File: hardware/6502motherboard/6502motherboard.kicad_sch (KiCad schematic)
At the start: 21 parts, among them J1 AUX 5VDC, J2 POWER 5V, J3 GND, SW1 POWER, U3 74HCT273

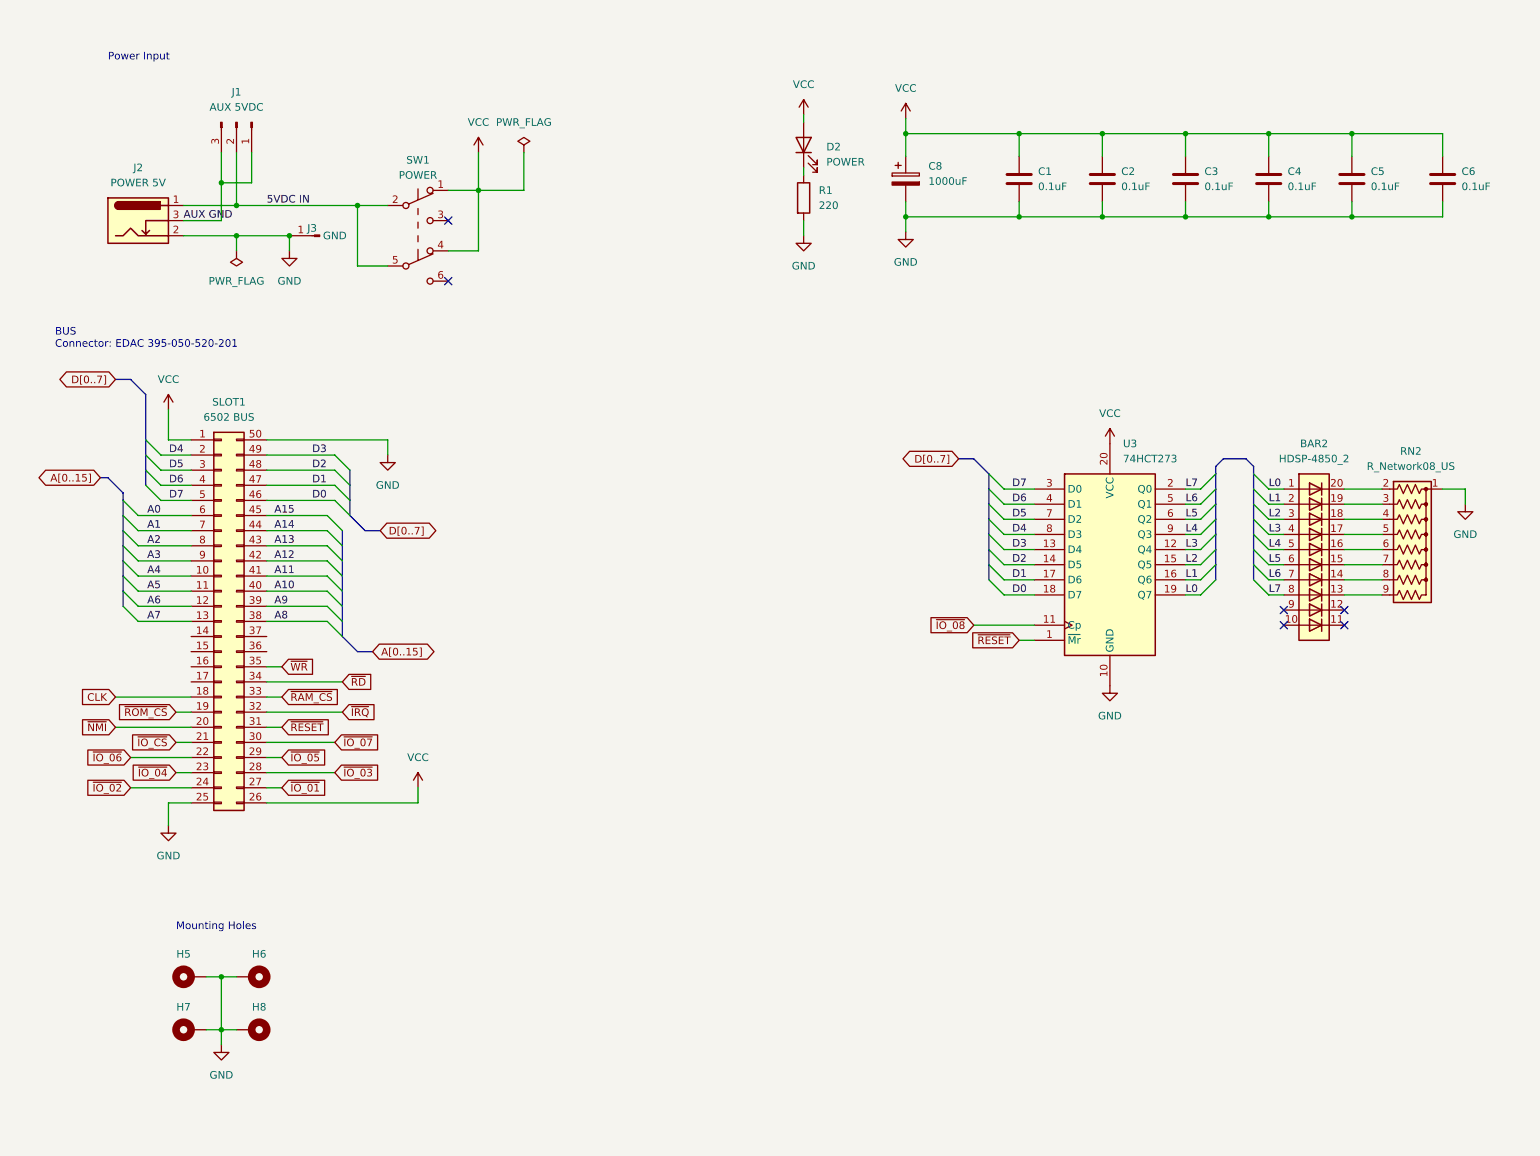
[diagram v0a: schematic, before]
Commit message: Fixed 6502 Pinout, routed bus and power
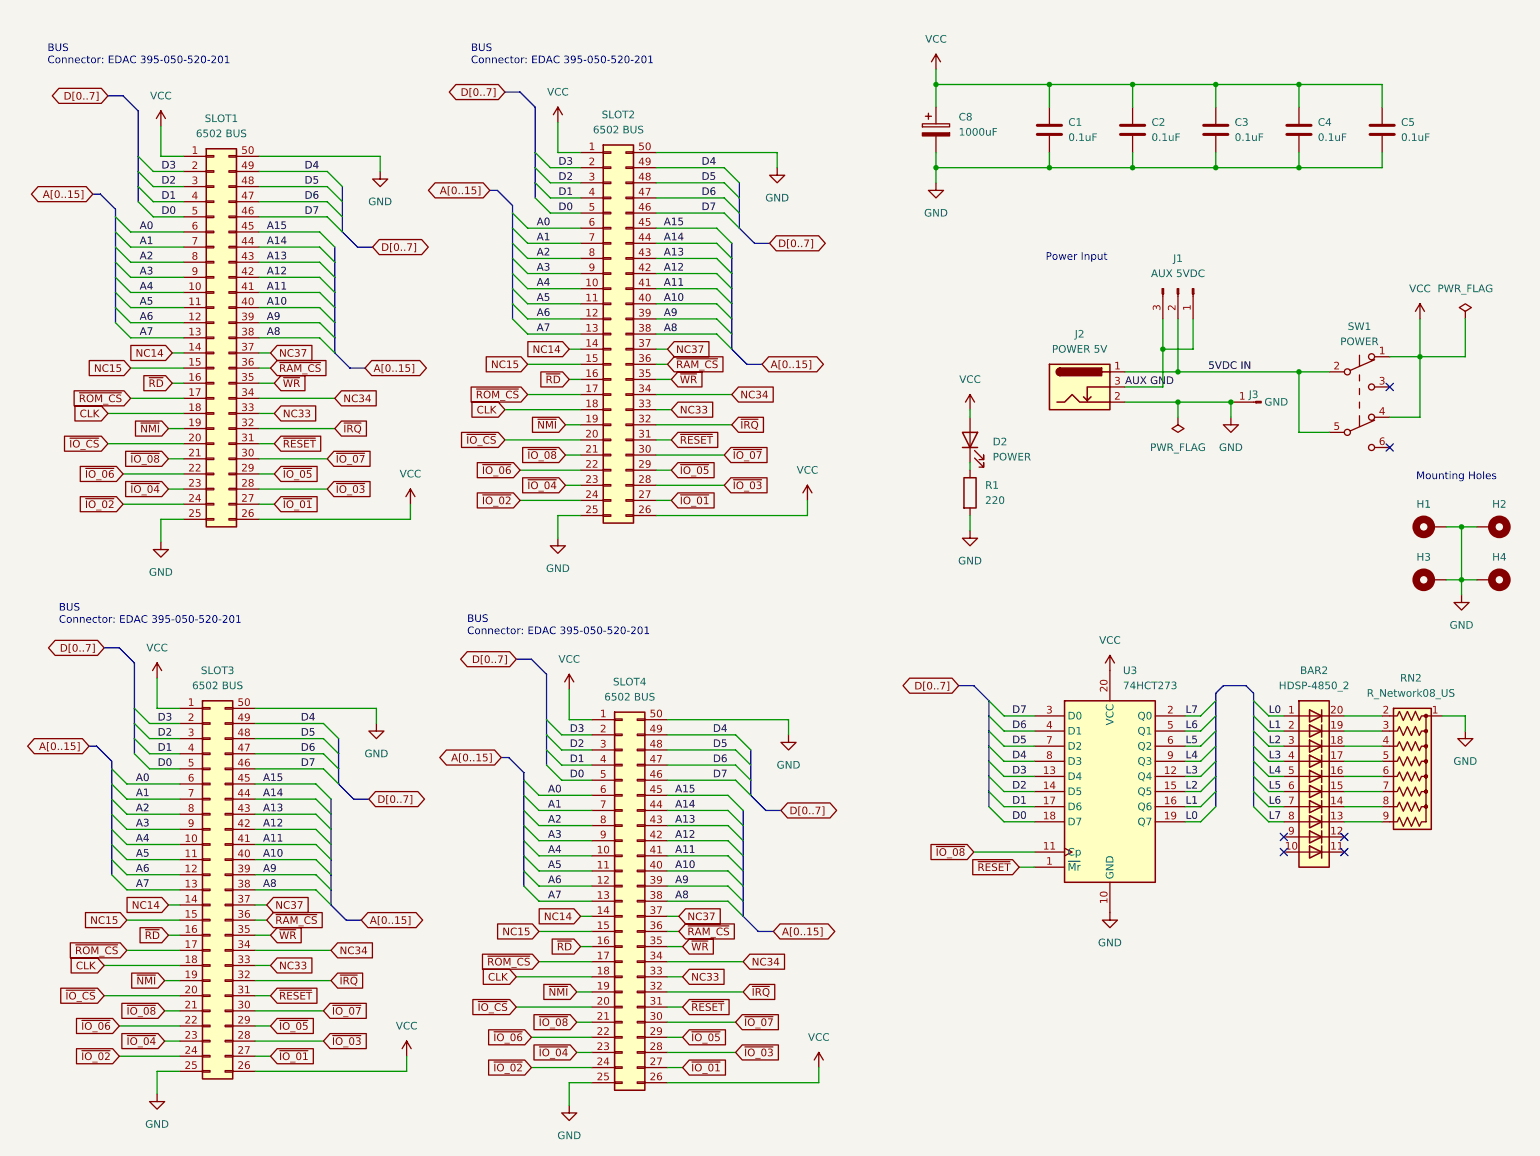
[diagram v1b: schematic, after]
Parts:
- removed C6: 0.1uF, Capacitor_THT:C_Disc_D3.0mm_W1.6mm_P2.50mm, symbol Device:C
- added SLOT2, SLOT3, SLOT4: 6502 BUS, Connector_Card:EDAC 395-050-520-201, symbol Connector_Generic:Conn_02x25_Counter_Clockwise
- renumbered H5 to H1, H6 to H2, H7 to H3, H8 to H4
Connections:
- net A0: now also SLOT2.6 (Pin_6), SLOT3.6 (Pin_6), SLOT4.6 (Pin_6)
- net A1: now also SLOT2.7 (Pin_7), SLOT3.7 (Pin_7), SLOT4.7 (Pin_7)
- net A10: now also SLOT2.40 (Pin_40), SLOT3.40 (Pin_40), SLOT4.40 (Pin_40)
- net A11: now also SLOT2.41 (Pin_41), SLOT3.41 (Pin_41), SLOT4.41 (Pin_41)
- net A12: now also SLOT2.42 (Pin_42), SLOT3.42 (Pin_42), SLOT4.42 (Pin_42)
- net A13: now also SLOT2.43 (Pin_43), SLOT3.43 (Pin_43), SLOT4.43 (Pin_43)
- net A14: now also SLOT2.44 (Pin_44), SLOT3.44 (Pin_44), SLOT4.44 (Pin_44)
- net A15: now also SLOT2.45 (Pin_45), SLOT3.45 (Pin_45), SLOT4.45 (Pin_45)
- net A2: now also SLOT2.8 (Pin_8), SLOT3.8 (Pin_8), SLOT4.8 (Pin_8)
- net A3: now also SLOT2.9 (Pin_9), SLOT3.9 (Pin_9), SLOT4.9 (Pin_9)
- net A4: now also SLOT2.10 (Pin_10), SLOT3.10 (Pin_10), SLOT4.10 (Pin_10)
- net A5: now also SLOT2.11 (Pin_11), SLOT3.11 (Pin_11), SLOT4.11 (Pin_11)
- net A6: now also SLOT2.12 (Pin_12), SLOT3.12 (Pin_12), SLOT4.12 (Pin_12)
- net A7: now also SLOT2.13 (Pin_13), SLOT3.13 (Pin_13), SLOT4.13 (Pin_13)
- net A8: now also SLOT2.38 (Pin_38), SLOT3.38 (Pin_38), SLOT4.38 (Pin_38)
- net A9: now also SLOT2.39 (Pin_39), SLOT3.39 (Pin_39), SLOT4.39 (Pin_39)
- net CLK: now also SLOT2.18 (Pin_18), SLOT3.18 (Pin_18), SLOT4.18 (Pin_18)
- net D0: now also SLOT1.5 (Pin_5), SLOT2.5 (Pin_5), SLOT3.5 (Pin_5), SLOT4.5 (Pin_5); no longer SLOT1.46 (Pin_46)
- net D1: now also SLOT1.4 (Pin_4), SLOT2.4 (Pin_4), SLOT3.4 (Pin_4), SLOT4.4 (Pin_4); no longer SLOT1.47 (Pin_47)
- net D2: now also SLOT1.3 (Pin_3), SLOT2.3 (Pin_3), SLOT3.3 (Pin_3), SLOT4.3 (Pin_3); no longer SLOT1.48 (Pin_48)
- net D3: now also SLOT1.2 (Pin_2), SLOT2.2 (Pin_2), SLOT3.2 (Pin_2), SLOT4.2 (Pin_2); no longer SLOT1.49 (Pin_49)
- net D4: now also SLOT1.49 (Pin_49), SLOT2.49 (Pin_49), SLOT3.49 (Pin_49), SLOT4.49 (Pin_49); no longer SLOT1.2 (Pin_2)
- net D5: now also SLOT1.48 (Pin_48), SLOT2.48 (Pin_48), SLOT3.48 (Pin_48), SLOT4.48 (Pin_48); no longer SLOT1.3 (Pin_3)
- net D6: now also SLOT1.47 (Pin_47), SLOT2.47 (Pin_47), SLOT3.47 (Pin_47), SLOT4.47 (Pin_47); no longer SLOT1.4 (Pin_4)
- net D7: now also SLOT1.46 (Pin_46), SLOT2.46 (Pin_46), SLOT3.46 (Pin_46), SLOT4.46 (Pin_46); no longer SLOT1.5 (Pin_5)
- net GND: now also SLOT2.25 (Pin_25), SLOT2.50 (Pin_50), SLOT3.25 (Pin_25), SLOT3.50 (Pin_50), SLOT4.25 (Pin_25), SLOT4.50 (Pin_50)
- net VCC: now also SLOT2.1 (Pin_1), SLOT2.26 (Pin_26), SLOT3.1 (Pin_1), SLOT3.26 (Pin_26), SLOT4.1 (Pin_1), SLOT4.26 (Pin_26)
- net ~{IO_01}: now also SLOT2.27 (Pin_27), SLOT3.27 (Pin_27), SLOT4.27 (Pin_27)
- net ~{IO_02}: now also SLOT2.24 (Pin_24), SLOT3.24 (Pin_24), SLOT4.24 (Pin_24)
- net ~{IO_03}: now also SLOT2.28 (Pin_28), SLOT3.28 (Pin_28), SLOT4.28 (Pin_28)
- net ~{IO_04}: now also SLOT2.23 (Pin_23), SLOT3.23 (Pin_23), SLOT4.23 (Pin_23)
- net ~{IO_05}: now also SLOT2.29 (Pin_29), SLOT3.29 (Pin_29), SLOT4.29 (Pin_29)
- net ~{IO_06}: now also SLOT2.22 (Pin_22), SLOT3.22 (Pin_22), SLOT4.22 (Pin_22)
- net ~{IO_07}: now also SLOT2.30 (Pin_30), SLOT3.30 (Pin_30), SLOT4.30 (Pin_30)
- net ~{IO_08}: now also SLOT1.21 (Pin_21), SLOT2.21 (Pin_21), SLOT3.21 (Pin_21), SLOT4.21 (Pin_21)
- net ~{IO_CS}: now also SLOT1.20 (Pin_20), SLOT2.20 (Pin_20), SLOT3.20 (Pin_20), SLOT4.20 (Pin_20); no longer SLOT1.21 (Pin_21)
- net ~{IRQ}: now also SLOT2.32 (Pin_32), SLOT3.32 (Pin_32), SLOT4.32 (Pin_32)
- net ~{NMI}: now also SLOT1.19 (Pin_19), SLOT2.19 (Pin_19), SLOT3.19 (Pin_19), SLOT4.19 (Pin_19); no longer SLOT1.20 (Pin_20)
- net ~{RAM_CS}: now also SLOT1.36 (Pin_36), SLOT2.36 (Pin_36), SLOT3.36 (Pin_36), SLOT4.36 (Pin_36); no longer SLOT1.33 (Pin_33)
- net ~{RD}: now also SLOT1.16 (Pin_16), SLOT2.16 (Pin_16), SLOT3.16 (Pin_16), SLOT4.16 (Pin_16); no longer SLOT1.34 (Pin_34)
- net ~{RESET}: now also SLOT2.31 (Pin_31), SLOT3.31 (Pin_31), SLOT4.31 (Pin_31)
- net ~{ROM_CS}: now also SLOT1.17 (Pin_17), SLOT2.17 (Pin_17), SLOT3.17 (Pin_17), SLOT4.17 (Pin_17); no longer SLOT1.19 (Pin_19)
- net ~{WR}: now also SLOT2.35 (Pin_35), SLOT3.35 (Pin_35), SLOT4.35 (Pin_35)
- net NC14: now reaches SLOT1.14 (Pin_14)
- net NC14: now also SLOT2.14 (Pin_14), SLOT3.14 (Pin_14), SLOT4.14 (Pin_14)
- net NC15: now reaches SLOT1.15 (Pin_15)
- net NC15: now also SLOT2.15 (Pin_15), SLOT3.15 (Pin_15), SLOT4.15 (Pin_15)
- net NC37: now reaches SLOT1.37 (Pin_37)
- net NC37: now also SLOT2.37 (Pin_37), SLOT3.37 (Pin_37), SLOT4.37 (Pin_37)
- new net NC33: SLOT1.33 (Pin_33), SLOT2.33 (Pin_33), SLOT3.33 (Pin_33), SLOT4.33 (Pin_33)
- new net NC34: SLOT1.34 (Pin_34), SLOT2.34 (Pin_34), SLOT3.34 (Pin_34), SLOT4.34 (Pin_34)
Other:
- moved on the sheet: BAR2, C1, C2, C3, C4, C5, C8, D2, H1, H2, H3, H4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

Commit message: v1.0 Motherboard Ready
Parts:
- added SW2: SW_Push, Button_Switch_THT:SW_PUSH_6mm_H5mm, symbol Switch:SW_Push
- added T1: DS-1813, Package_TO_SOT_THT:21-0248A_MAXIM, symbol Mariano Extras:DS-1813
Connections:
- net GND: now also SW2.2, T1.3 (GND)
- net VCC: now also T1.2 (VCC)
- net ~{RESET}: now also SW2.1, T1.1 (~{RST})
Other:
- moved on the sheet: D2, R1

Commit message: v1.6 Motherboard Complete
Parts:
- removed D2: POWER, LED_THT:LED_D3.0mm, symbol Device:LED
- removed R1: 220, Resistor_THT:R_Axial_DIN0204_L3.6mm_D1.6mm_P7.62mm_Horizontal, symbol Device:R
- added R2: 220, Resistor_THT:R_Axial_DIN0204_L3.6mm_D1.6mm_P7.62mm_Horizontal, symbol Device:R
- added SLOT5: 6502 BUS, Connector_PinHeader_2.54mm:PinHeader_2x25_P2.54mm_Vertical_Counter_Clockwise, symbol Connector_Generic:Conn_02x25_Counter_Clockwise
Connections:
- net A0: now also SLOT5.6 (Pin_6)
- net A1: now also SLOT5.7 (Pin_7)
- net A10: now also SLOT5.40 (Pin_40)
- net A11: now also SLOT5.41 (Pin_41)
- net A12: now also SLOT5.42 (Pin_42)
- net A13: now also SLOT5.43 (Pin_43)
- net A14: now also SLOT5.44 (Pin_44)
- net A15: now also SLOT5.45 (Pin_45)
- net A2: now also SLOT5.8 (Pin_8)
- net A3: now also SLOT5.9 (Pin_9)
- net A4: now also SLOT5.10 (Pin_10)
- net A5: now also SLOT5.11 (Pin_11)
- net A6: now also SLOT5.12 (Pin_12)
- net A7: now also SLOT5.13 (Pin_13)
- net A8: now also SLOT5.38 (Pin_38)
- net A9: now also SLOT5.39 (Pin_39)
- net CLK: now also SLOT5.18 (Pin_18)
- net D0: now also SLOT5.5 (Pin_5)
- net D1: now also SLOT5.4 (Pin_4)
- net D2: now also SLOT5.3 (Pin_3)
- net D3: now also SLOT5.2 (Pin_2)
- net D4: now also SLOT5.49 (Pin_49)
- net D5: now also SLOT5.48 (Pin_48)
- net D6: now also SLOT5.47 (Pin_47)
- net D7: now also SLOT5.46 (Pin_46)
- net GND: now also R2.2, SLOT5.25 (Pin_25), SLOT5.50 (Pin_50)
- net NC14: now also SLOT5.14 (Pin_14)
- net NC15: now also SLOT5.15 (Pin_15)
- net NC33: now also SLOT5.33 (Pin_33)
- net NC34: now also SLOT5.34 (Pin_34)
- net NC37: now also SLOT5.37 (Pin_37)
- net VCC: now also BAR2.11 (K), SLOT5.1 (Pin_1), SLOT5.26 (Pin_26)
- net ~{IO_01}: now also SLOT5.27 (Pin_27)
- net ~{IO_02}: now also SLOT5.24 (Pin_24)
- net ~{IO_03}: now also SLOT5.28 (Pin_28)
- net ~{IO_04}: now also SLOT5.23 (Pin_23)
- net ~{IO_05}: now also SLOT5.29 (Pin_29)
- net ~{IO_06}: now also SLOT5.22 (Pin_22)
- net ~{IO_07}: now also SLOT5.30 (Pin_30)
- net ~{IO_08}: now also SLOT5.21 (Pin_21)
- net ~{IO_CS}: now also SLOT5.20 (Pin_20)
- net ~{IRQ}: now also SLOT5.32 (Pin_32)
- net ~{NMI}: now also SLOT5.19 (Pin_19)
- net ~{RAM_CS}: now also SLOT5.36 (Pin_36)
- net ~{RD}: now also SLOT5.16 (Pin_16)
- net ~{RESET}: now also SLOT5.31 (Pin_31)
- net ~{ROM_CS}: now also SLOT5.17 (Pin_17)
- net ~{WR}: now also SLOT5.35 (Pin_35)
- net at BAR2.10 (A): now also R2.1
- no-connect marks 6 -> 4
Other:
- moved on the sheet: BAR2, C1, C2, C3, C4, C5, C8, H1, H2, H3, H4, J1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

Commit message: Motherboard added 7805 regulator
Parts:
- added C6: 100nF, Capacitor_THT:C_Disc_D3.0mm_W1.6mm_P2.50mm, symbol Device:C_Small
- added C7: 330nF, Capacitor_THT:C_Disc_D3.0mm_W1.6mm_P2.50mm, symbol Device:C_Small
- added J4: NO 7502, Connector_PinHeader_2.54mm:PinHeader_1x03_P2.54mm_Vertical, symbol Connector:Conn_01x03_Pin
- added U1: LM7805_TO220, Package_TO_SOT_THT:TO-220-3_Horizontal_TabDown, symbol Regulator_Linear:LM7805_TO220
- C8: value 1000uF -> 10uF
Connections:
- net GND: now also C6.2, C7.2, U1.2 (GND)
- net VCC: now also BAR2.10 (A), C6.1, J4.3 (Pin_3), U1.3 (VO); no longer BAR2.11 (K), SW1.1 (A), SW1.4 (A)
- net at R2.1: now also BAR2.11 (K); no longer BAR2.10 (A)
- net 5VDC IN renamed VDC
- new net VDC_IN: J4.2 (Pin_2), SW1.1 (A), SW1.4 (A)
- new net V_IN: C7.1, J4.1 (Pin_1), U1.1 (VI)
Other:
- moved on the sheet: J1, J2, J3, R2, SW1

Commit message: I_O8 Jumper and more PCB cleanup
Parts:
- added J5: IO_8, Connector_PinHeader_2.54mm:PinHeader_1x02_P2.54mm_Vertical, symbol Connector:Conn_01x02_Pin
- U1: value LM7805_TO220 -> LM7805
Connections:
- net ~{IO_08}: now also J5.2 (Pin_2); no longer U3.11 (Cp)
- new net ~{U3_CS}: J5.1 (Pin_1), U3.11 (Cp)
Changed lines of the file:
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@@
     (stroke (width 0) (type default))
   )
+  (wire (pts (xy 170.815 153.67) (xy 170.815 154.94))
+    (stroke (width 0) (type default))
+  )
   (wire (pts (xy 36.195 96.52) (xy 36.195 100.33))
     (stroke (width 0) (type default))
@@
     (stroke (width 0) (type default))
   )
+  (wire (pts (xy 165.1 154.94) (xy 168.275 154.94))
+    (stroke (width 0) (type default))
+  )
   (wire (pts (xy 144.78 93.345) (xy 144.78 95.885))
     (stroke (width 0) (type default))
@@
     (stroke (width 0) (type default))
   )
+  (wire (pts (xy 168.275 153.67) (xy 168.275 154.94))
+    (stroke (width 0) (type default))
+  )
   (wire (pts (xy 175.895 105.41) (xy 179.07 105.41))
     (stroke (width 0) (type default))
@@
     (stroke (width 0) (type default))
   )
-  (wire (pts (xy 173.99 154.94) (xy 184.15 154.94))
+  (wire (pts (xy 170.815 154.94) (xy 184.15 154.94))
     (stroke (width 0) (type default))
   )
@@
     (effects (font (size 1.27 1.27)) (justify left bottom))
   )
+  (label "~{U3_CS}" (at 176.53 154.94 0) (fields_autoplaced)
+    (effects (font (size 1.27 1.27)) (justify left bottom))
+  )
   (label "A13" (at 53.34 146.05 0) (fields_autoplaced)
     (effects (font (size 1.27 1.27)) (justify left bottom))
@@
     )
   )
-  (global_label "~{IO_08}" (shape input) (at 173.99 154.94 180) (fields_autoplaced)
+  (global_label "~{IO_08}" (shape input) (at 165.1 154.94 180) (fields_autoplaced)
     (effects (font (size 1.27 1.27)) (justify right))
-    (property "Intersheetrefs" "${INTERSHEET_REFS}" (at 165.6829 154.94 0)
+    (property "Intersheetrefs" "${INTERSHEET_REFS}" (at 156.7929 154.94 0)
       (effects (font (size 1.27 1.27)) (justify right) hide)
     )
@@
     )
   )
+  (symbol (lib_id "Connector:Conn_01x02_Pin") (at 170.815 148.59 270) (unit 1)
+    (in_bom yes) (on_board yes) (dnp no) (fields_autoplaced)
+    (property "Reference" "J5" (at 172.085 147.955 90)
+      (effects (font (size 1.27 1.27)) (justify left))
+    )
+    (property "Value" "IO_8" (at 172.085 150.495 90)
+      (effects (font (size 1.27 1.27)) (justify left))
+    )
+    (property "Footprint" "Connector_PinHeader_2.54mm:PinHeader_1x02_P2.54mm_Vertical" (at 170.815 148.59 0)
+      (effects (font (size 1.27 1.27)) hide)
+    )
+    (property "Datasheet" "~" (at 170.815 148.59 0)
+      (effects (font (size 1.27 1.27)) hide)
+    )
+    (pin "1")
+    (pin "2")
+    (instances
+      (project "6502motherboard"
+        (path "/79b045e9-6697-4ebd-8cd3-5e519b22df02"
+          (reference "J5") (unit 1)
+        )
+      )
+    )
+  )
   (symbol (lib_id "Connector:Conn_01x01_Pin") (at 230.505 111.125 180) (unit 1)
     (in_bom yes) (on_board yes) (dnp no)
@@
       (effects (font (size 1.27 1.27)))
     )
-    (property "Value" "LM7805_TO220" (at 229.87 77.47 0)
+    (property "Value" "LM7805" (at 229.87 77.47 0)
       (effects (font (size 1.27 1.27)))
     )
